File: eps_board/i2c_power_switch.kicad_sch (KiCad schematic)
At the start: 6 parts, among them U25 MCP23008T-E/SS

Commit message: changed from 48 pin connector to 40 pic PCA connector. remove uarts, ensure reset pins for all system components, attention pin to iniate IRQ on all components
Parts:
- renumbered C67 to C58, R110 to R107, R111 to R108, R112 to R109, R113 to R110, U25 to U21
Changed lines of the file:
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@@
 	(wire
 		(pts
-			(xy 43.18 34.29) (xy 37.465 34.29)
+			(xy 37.465 49.53) (xy 64.77 49.53)
 		)
 		(stroke
@@
 		(pts
 			(xy 167.005 103.505) (xy 168.91 103.505)
-		)
-		(stroke
-			(width 0)
-			(type default)
-		)
-	)
-	(wire
-		(pts
-			(xy 60.96 49.53) (xy 64.77 49.53)
 		)
 		(stroke
@@
 		)
 	)
-	(label "INT_VIN"
-		(at 43.18 34.29 0)
-		(fields_autoplaced yes)
-		(effects
-			(font
-				(size 1.27 1.27)
-			)
-			(justify left bottom)
-		)
-	)
 	(label "ENABLE2"
 		(at 100.33 46.99 0)
@@
 		)
 	)
-	(label "SDA_VIN"
+	(label "SDA"
 		(at 139.065 81.28 180)
 		(fields_autoplaced yes)
@@
 		)
 	)
-	(label "SDA_VIN"
+	(label "SDA"
 		(at 138.43 115.57 180)
 		(fields_autoplaced yes)
@@
 		)
 	)
-	(label "SDA_VIN"
+	(label "SDA"
 		(at 130.81 111.76 180)
 		(fields_autoplaced yes)
@@
 		)
 	)
-	(label "SCL_VIN"
+	(label "SCL"
 		(at 138.43 153.035 180)
 		(fields_autoplaced yes)
@@
 		)
 	)
-	(label "SCL_VIN"
+	(label "SCL"
 		(at 139.065 49.53 180)
 		(fields_autoplaced yes)
@@
 		)
 	)
-	(label "SCL_VIN"
+	(label "SCL"
 		(at 130.175 146.685 180)
 		(fields_autoplaced yes)
@@
 		)
 	)
-	(label "SDA_VIN"
-		(at 54.61 34.29 0)
-		(fields_autoplaced yes)
-		(effects
-			(font
-				(size 1.27 1.27)
-			)
-			(justify left bottom)
-		)
-	)
 	(label "ENABLE1"
 		(at 100.33 41.91 0)
@@
 		)
 	)
-	(label "SDA_VIN"
+	(label "SDA"
 		(at 138.43 150.495 180)
 		(fields_autoplaced yes)
@@
 		)
 	)
-	(label "SCL_VIN"
-		(at 52.705 31.75 0)
-		(fields_autoplaced yes)
-		(effects
-			(font
-				(size 1.27 1.27)
-			)
-			(justify left bottom)
-		)
-	)
-	(label "SCL_VIN"
+	(label "SCL"
 		(at 139.065 83.82 180)
 		(fields_autoplaced yes)
@@
 		)
 	)
-	(label "INT_VIN"
-		(at 60.96 49.53 180)
+	(label "SCL"
+		(at 138.43 118.11 180)
 		(fields_autoplaced yes)
 		(effects
@@
 		)
 	)
-	(label "SCL_VIN"
-		(at 138.43 118.11 180)
-		(fields_autoplaced yes)
-		(effects
-			(font
-				(size 1.27 1.27)
-			)
-			(justify right bottom)
-		)
-	)
-	(label "SDA_VIN"
+	(label "SDA"
 		(at 139.065 46.99 180)
 		(fields_autoplaced yes)
@@
 	(hierarchical_label "INT"
 		(shape input)
-		(at 37.465 34.29 180)
+		(at 37.465 49.53 180)
 		(fields_autoplaced yes)
 		(effects
@@
 		(dnp no)
 		(fields_autoplaced yes)
-		(property "Reference" "C67"
+		(property "Reference" "C58"
 			(at 121.285 40.0049 0)
 			(effects
@@
 			(project ""
 				(path "/05170af6-30ef-4c3a-b972-f098085da1bc/53211e67-c677-4be8-893d-9825fa308902"
-					(reference "C67")
+					(reference "C58")
 					(unit 1)
 				)
@@
 		(dnp no)
 		(fields_autoplaced yes)
-		(property "Reference" "R111"
+		(property "Reference" "R108"
 			(at 172.085 71.7549 0)
 			(effects
@@
 			(project "EPS"
 				(path "/05170af6-30ef-4c3a-b972-f098085da1bc/53211e67-c677-4be8-893d-9825fa308902"
-					(reference "R111")
+					(reference "R108")
 					(unit 1)
 				)
@@
 		(dnp no)
 		(fields_autoplaced yes)
-		(property "Reference" "R113"
+		(property "Reference" "R110"
 			(at 171.45 140.9699 0)
 			(effects
@@
 			(project "EPS"
 				(path "/05170af6-30ef-4c3a-b972-f098085da1bc/53211e67-c677-4be8-893d-9825fa308902"
-					(reference "R113")
+					(reference "R110")
 					(unit 1)
 				)
@@
 		(dnp no)
 		(fields_autoplaced yes)
-		(property "Reference" "R110"
+		(property "Reference" "R107"
 			(at 172.085 37.4649 0)
 			(effects
@@
 			(project "EPS"
 				(path "/05170af6-30ef-4c3a-b972-f098085da1bc/53211e67-c677-4be8-893d-9825fa308902"
-					(reference "R110")
+					(reference "R107")
 					(unit 1)
 				)
@@
 		(dnp no)
 		(fields_autoplaced yes)
-		(property "Reference" "R112"
+		(property "Reference" "R109"
 			(at 171.45 106.0449 0)
 			(effects
@@
 			(project "EPS"
 				(path "/05170af6-30ef-4c3a-b972-f098085da1bc/53211e67-c677-4be8-893d-9825fa308902"
-					(reference "R112")
+					(reference "R109")
 					(unit 1)
 				)
@@
 		(dnp no)
 		(fields_autoplaced yes)
-		(property "Reference" "U25"
+		(property "Reference" "U21"
 			(at 80.01 25.4 0)
 			(effects
@@
 			(project ""
 				(path "/05170af6-30ef-4c3a-b972-f098085da1bc/53211e67-c677-4be8-893d-9825fa308902"
-					(reference "U25")
+					(reference "U21")
 					(unit 1)
 				)

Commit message: simply eps and automate startup conditions
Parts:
- renumbered C58 to C75, R107 to R91, R108 to R92, R109 to R93, R110 to R94, U21 to U27
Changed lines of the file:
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@@
 	(wire
 		(pts
-			(xy 130.81 111.76) (xy 140.335 111.76)
+			(xy 138.43 111.76) (xy 140.335 111.76)
 		)
 		(stroke
@@
 	(wire
 		(pts
-			(xy 130.175 146.685) (xy 140.335 146.685)
+			(xy 138.43 146.685) (xy 140.335 146.685)
 		)
 		(stroke
@@
 		)
 	)
-	(label "SDA"
-		(at 139.065 81.28 180)
-		(fields_autoplaced yes)
-		(effects
-			(font
-				(size 1.27 1.27)
-			)
-			(justify right bottom)
-		)
-	)
-	(label "SDA"
-		(at 138.43 115.57 180)
-		(fields_autoplaced yes)
-		(effects
-			(font
-				(size 1.27 1.27)
-			)
-			(justify right bottom)
-		)
-	)
-	(label "SDA"
-		(at 130.81 111.76 180)
-		(fields_autoplaced yes)
-		(effects
-			(font
-				(size 1.27 1.27)
-			)
-			(justify right bottom)
-		)
-	)
 	(label "ENABLE3"
 		(at 168.91 151.765 0)
@@
 		)
 	)
-	(label "SCL"
-		(at 138.43 153.035 180)
-		(fields_autoplaced yes)
-		(effects
-			(font
-				(size 1.27 1.27)
-			)
-			(justify right bottom)
-		)
-	)
-	(label "SCL"
-		(at 139.065 49.53 180)
-		(fields_autoplaced yes)
-		(effects
-			(font
-				(size 1.27 1.27)
-			)
-			(justify right bottom)
-		)
-	)
-	(label "SCL"
-		(at 130.175 146.685 180)
-		(fields_autoplaced yes)
-		(effects
-			(font
-				(size 1.27 1.27)
-			)
-			(justify right bottom)
-		)
-	)
 	(label "INT3"
 		(at 168.91 154.305 0)
@@
 		)
 	)
-	(label "SDA"
-		(at 138.43 150.495 180)
-		(fields_autoplaced yes)
-		(effects
-			(font
-				(size 1.27 1.27)
-			)
-			(justify right bottom)
-		)
-	)
-	(label "SCL"
-		(at 139.065 83.82 180)
-		(fields_autoplaced yes)
-		(effects
-			(font
-				(size 1.27 1.27)
-			)
-			(justify right bottom)
-		)
-	)
 	(label "ENABLE0"
 		(at 169.545 48.26 0)
@@
 		)
 	)
-	(label "SCL"
-		(at 138.43 118.11 180)
-		(fields_autoplaced yes)
-		(effects
-			(font
-				(size 1.27 1.27)
-			)
-			(justify right bottom)
-		)
-	)
-	(label "SDA"
-		(at 139.065 46.99 180)
-		(fields_autoplaced yes)
-		(effects
-			(font
-				(size 1.27 1.27)
-			)
-			(justify right bottom)
-		)
-	)
 	(label "INT0"
 		(at 100.33 34.29 0)
@@
 		(shape input)
 		(at 139.065 41.275 180)
+		(fields_autoplaced yes)
+		(effects
+			(font
+				(size 1.27 1.27)
+			)
+			(justify right)
+		)
+	)
+	(hierarchical_label "SCL"
+		(shape input)
+		(at 139.065 49.53 180)
 		(fields_autoplaced yes)
 		(effects
@@
 		)
 	)
+	(hierarchical_label "SDA"
+		(shape input)
+		(at 138.43 115.57 180)
+		(fields_autoplaced yes)
+		(effects
+			(font
+				(size 1.27 1.27)
+			)
+			(justify right)
+		)
+	)
+	(hierarchical_label "SDA"
+		(shape input)
+		(at 138.43 111.76 180)
+		(fields_autoplaced yes)
+		(effects
+			(font
+				(size 1.27 1.27)
+			)
+			(justify right)
+		)
+	)
 	(hierarchical_label "GND"
 		(shape input)
@@
 		)
 	)
+	(hierarchical_label "SCL"
+		(shape input)
+		(at 138.43 153.035 180)
+		(fields_autoplaced yes)
+		(effects
+			(font
+				(size 1.27 1.27)
+			)
+			(justify right)
+		)
+	)
 	(hierarchical_label "GND"
 		(shape input)
 		(at 138.43 102.87 180)
+		(fields_autoplaced yes)
+		(effects
+			(font
+				(size 1.27 1.27)
+			)
+			(justify right)
+		)
+	)
+	(hierarchical_label "SCL"
+		(shape input)
+		(at 138.43 118.11 180)
 		(fields_autoplaced yes)
 		(effects
@@
 		)
 	)
+	(hierarchical_label "SCL"
+		(shape input)
+		(at 138.43 146.685 180)
+		(fields_autoplaced yes)
+		(effects
+			(font
+				(size 1.27 1.27)
+			)
+			(justify right)
+		)
+	)
 	(hierarchical_label "GND"
 		(shape input)
@@
 		)
 	)
+	(hierarchical_label "SDA"
+		(shape input)
+		(at 139.065 46.99 180)
+		(fields_autoplaced yes)
+		(effects
+			(font
+				(size 1.27 1.27)
+			)
+			(justify right)
+		)
+	)
+	(hierarchical_label "SDA"
+		(shape input)
+		(at 139.065 81.28 180)
+		(fields_autoplaced yes)
+		(effects
+			(font
+				(size 1.27 1.27)
+			)
+			(justify right)
+		)
+	)
 	(hierarchical_label "GND"
 		(shape input)
@@
 			)
 			(justify left)
+		)
+	)
+	(hierarchical_label "SDA"
+		(shape input)
+		(at 138.43 150.495 180)
+		(fields_autoplaced yes)
+		(effects
+			(font
+				(size 1.27 1.27)
+			)
+			(justify right)
 		)
 	)
@@
 		(shape input)
 		(at 64.77 36.83 180)
+		(fields_autoplaced yes)
+		(effects
+			(font
+				(size 1.27 1.27)
+			)
+			(justify right)
+		)
+	)
+	(hierarchical_label "SCL"
+		(shape input)
+		(at 139.065 83.82 180)
 		(fields_autoplaced yes)
 		(effects
@@
 		(dnp no)
 		(fields_autoplaced yes)
-		(property "Reference" "C58"
+		(property "Reference" "C75"
 			(at 121.285 40.0049 0)
 			(effects
@@
 			(project ""
 				(path "/05170af6-30ef-4c3a-b972-f098085da1bc/53211e67-c677-4be8-893d-9825fa308902"
-					(reference "C58")
+					(reference "C75")
 					(unit 1)
 				)
@@
 		(dnp no)
 		(fields_autoplaced yes)
-		(property "Reference" "R108"
+		(property "Reference" "R92"
 			(at 172.085 71.7549 0)
 			(effects
@@
 			(project "EPS"
 				(path "/05170af6-30ef-4c3a-b972-f098085da1bc/53211e67-c677-4be8-893d-9825fa308902"
-					(reference "R108")
+					(reference "R92")
 					(unit 1)
 				)
@@
 		(dnp no)
 		(fields_autoplaced yes)
-		(property "Reference" "R110"
+		(property "Reference" "R94"
 			(at 171.45 140.9699 0)
 			(effects
@@
 			(project "EPS"
 				(path "/05170af6-30ef-4c3a-b972-f098085da1bc/53211e67-c677-4be8-893d-9825fa308902"
-					(reference "R110")
+					(reference "R94")
 					(unit 1)
 				)
@@
 		(dnp no)
 		(fields_autoplaced yes)
-		(property "Reference" "R107"
+		(property "Reference" "R91"
 			(at 172.085 37.4649 0)
 			(effects
@@
 			(project "EPS"
 				(path "/05170af6-30ef-4c3a-b972-f098085da1bc/53211e67-c677-4be8-893d-9825fa308902"
-					(reference "R107")
+					(reference "R91")
 					(unit 1)
 				)
@@
 		(dnp no)
 		(fields_autoplaced yes)
-		(property "Reference" "R109"
+		(property "Reference" "R93"
 			(at 171.45 106.0449 0)
 			(effects
@@
 			(project "EPS"
 				(path "/05170af6-30ef-4c3a-b972-f098085da1bc/53211e67-c677-4be8-893d-9825fa308902"
-					(reference "R109")
+					(reference "R93")
 					(unit 1)
 				)
@@
 		(dnp no)
 		(fields_autoplaced yes)
-		(property "Reference" "U21"
+		(property "Reference" "U27"
 			(at 80.01 25.4 0)
 			(effects
@@
 			(project ""
 				(path "/05170af6-30ef-4c3a-b972-f098085da1bc/53211e67-c677-4be8-893d-9825fa308902"
-					(reference "U21")
+					(reference "U27")
 					(unit 1)
 				)

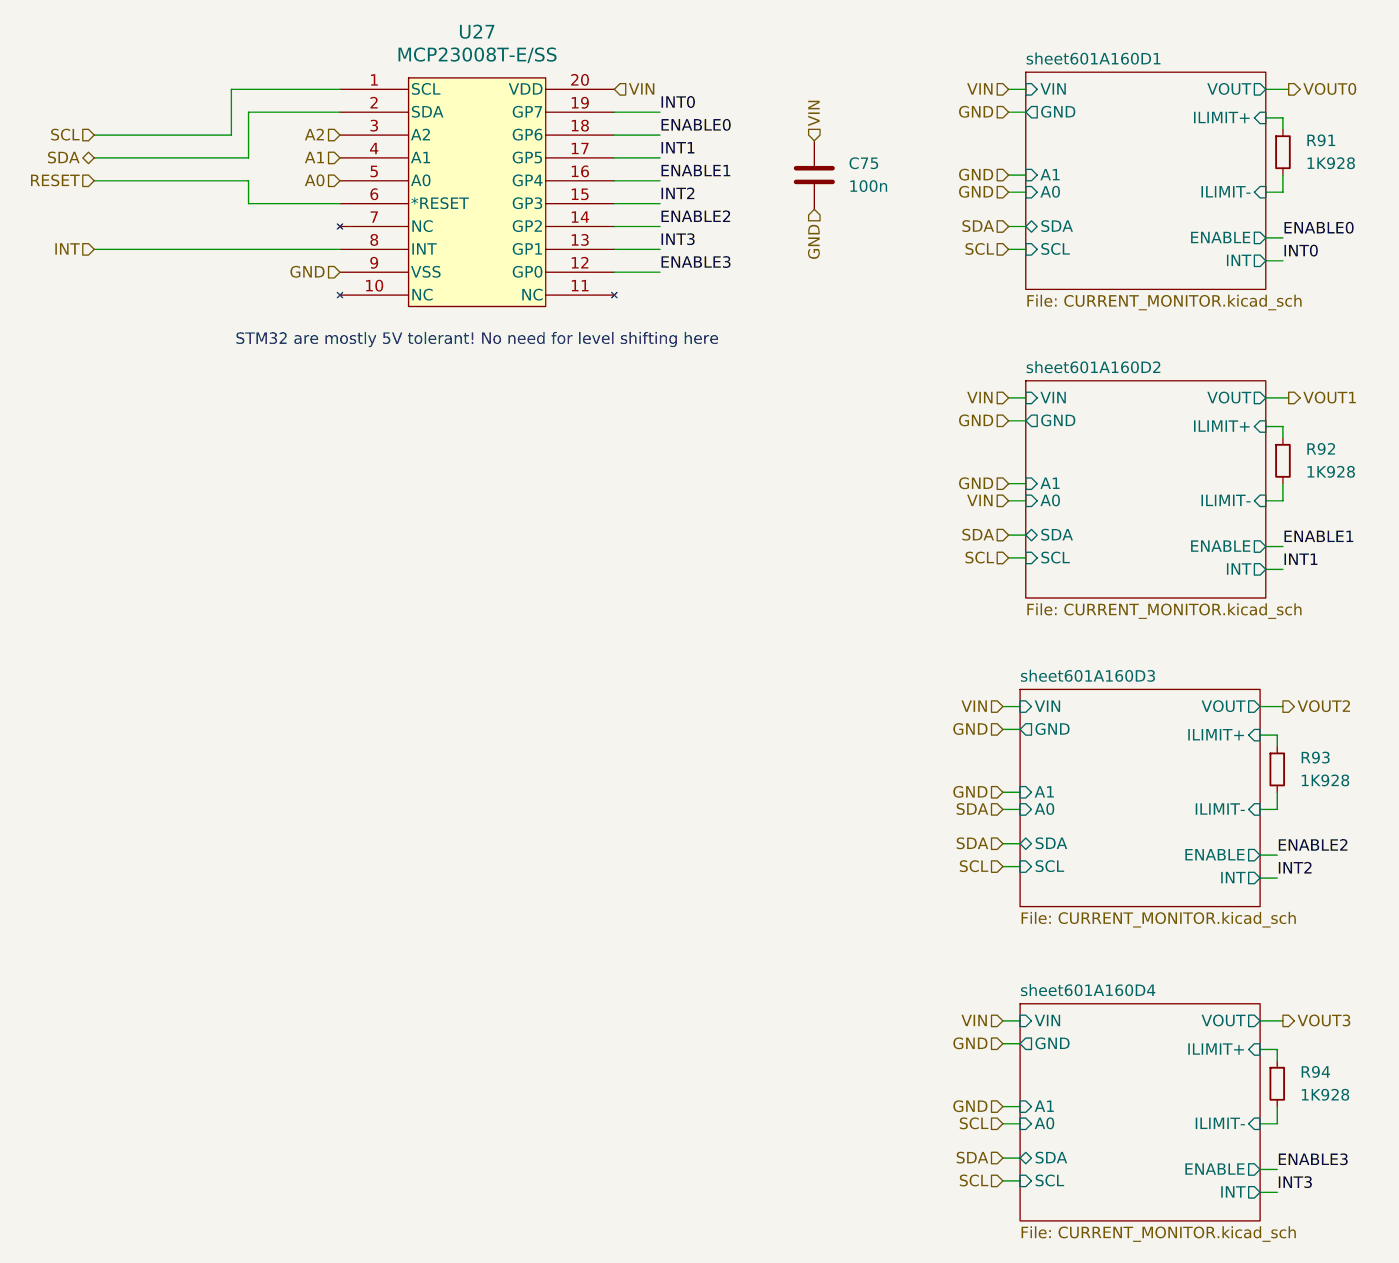
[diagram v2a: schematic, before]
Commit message: pcb and silk screen cleanup, interim
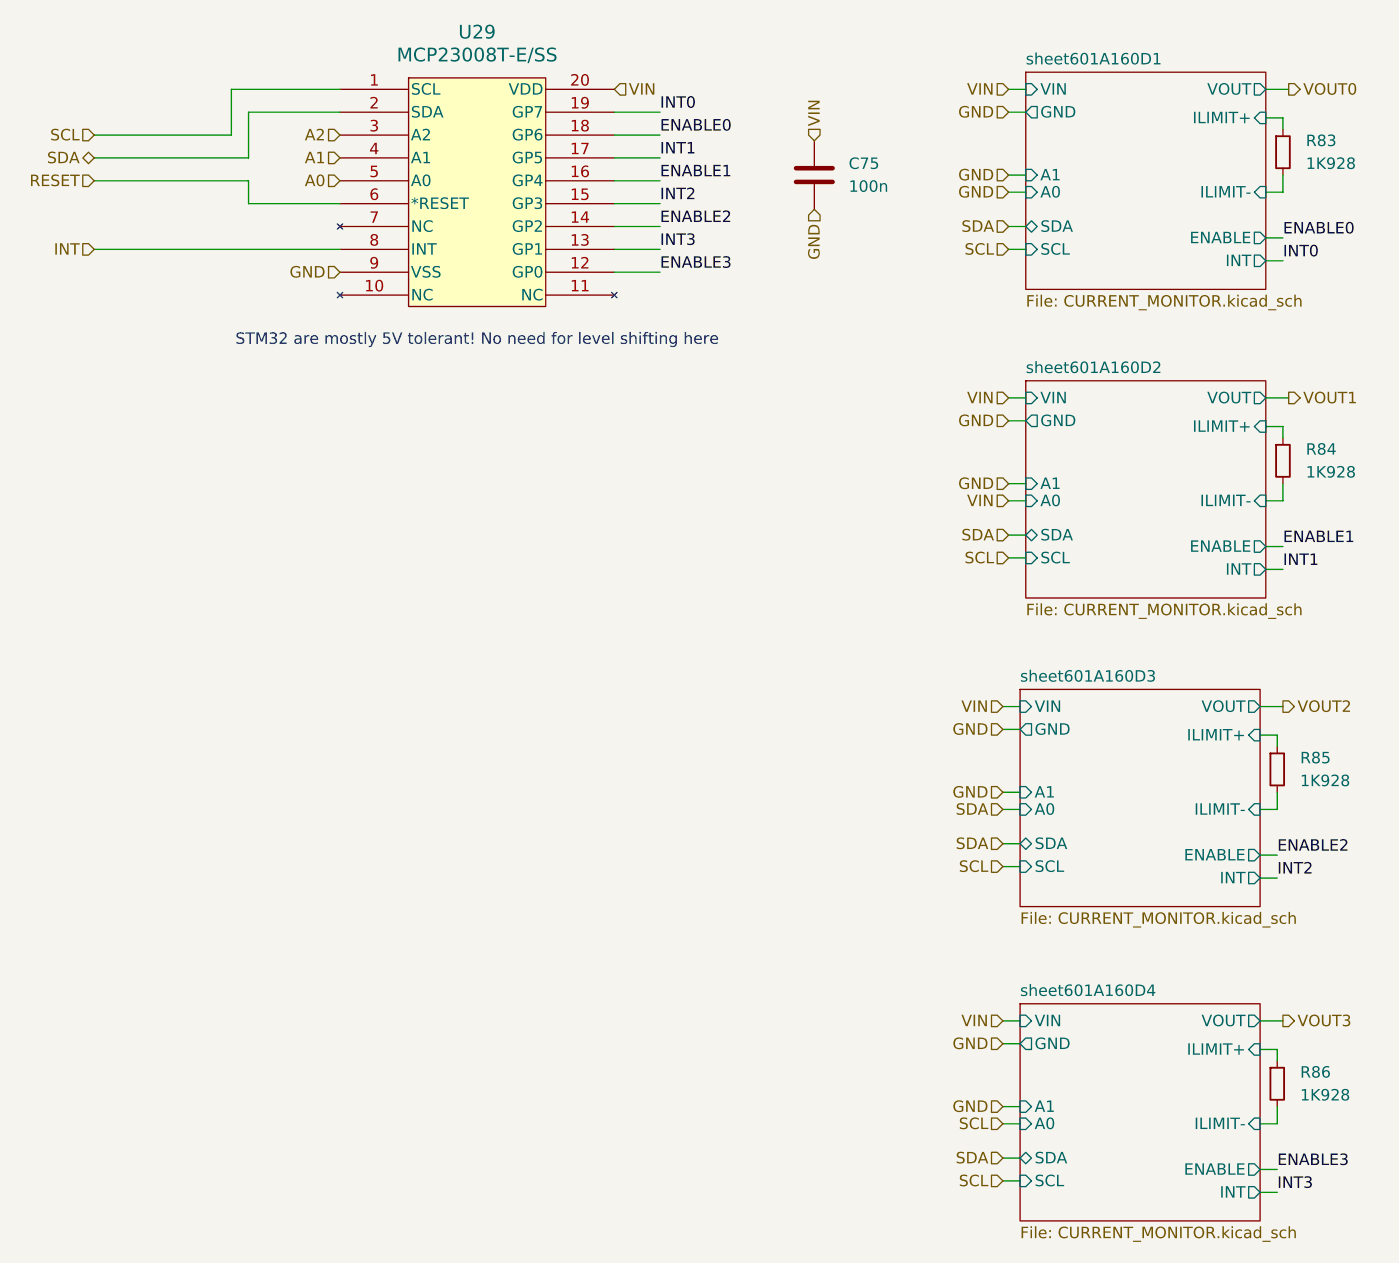
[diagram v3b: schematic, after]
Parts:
- renumbered R91 to R83, R92 to R84, R93 to R85, R94 to R86, U27 to U29
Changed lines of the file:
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@@
 		(dnp no)
 		(fields_autoplaced yes)
-		(property "Reference" "R92"
+		(property "Reference" "R84"
 			(at 172.085 71.7549 0)
 			(effects
@@
 			(project "EPS"
 				(path "/05170af6-30ef-4c3a-b972-f098085da1bc/53211e67-c677-4be8-893d-9825fa308902"
-					(reference "R92")
+					(reference "R84")
 					(unit 1)
 				)
@@
 		(dnp no)
 		(fields_autoplaced yes)
-		(property "Reference" "R94"
+		(property "Reference" "R86"
 			(at 171.45 140.9699 0)
 			(effects
@@
 			(project "EPS"
 				(path "/05170af6-30ef-4c3a-b972-f098085da1bc/53211e67-c677-4be8-893d-9825fa308902"
-					(reference "R94")
+					(reference "R86")
 					(unit 1)
 				)
@@
 		(dnp no)
 		(fields_autoplaced yes)
-		(property "Reference" "R91"
+		(property "Reference" "R83"
 			(at 172.085 37.4649 0)
 			(effects
@@
 			(project "EPS"
 				(path "/05170af6-30ef-4c3a-b972-f098085da1bc/53211e67-c677-4be8-893d-9825fa308902"
-					(reference "R91")
+					(reference "R83")
 					(unit 1)
 				)
@@
 		(dnp no)
 		(fields_autoplaced yes)
-		(property "Reference" "R93"
+		(property "Reference" "R85"
 			(at 171.45 106.0449 0)
 			(effects
@@
 			(project "EPS"
 				(path "/05170af6-30ef-4c3a-b972-f098085da1bc/53211e67-c677-4be8-893d-9825fa308902"
-					(reference "R93")
+					(reference "R85")
 					(unit 1)
 				)
@@
 		(dnp no)
 		(fields_autoplaced yes)
-		(property "Reference" "U27"
+		(property "Reference" "U29"
 			(at 80.01 25.4 0)
 			(effects
@@
 			(project ""
 				(path "/05170af6-30ef-4c3a-b972-f098085da1bc/53211e67-c677-4be8-893d-9825fa308902"
-					(reference "U27")
-					(unit 1)
-				)
+					(reference "U29")
+					(unit 1)
+				)
